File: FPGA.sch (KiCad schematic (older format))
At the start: 38 parts

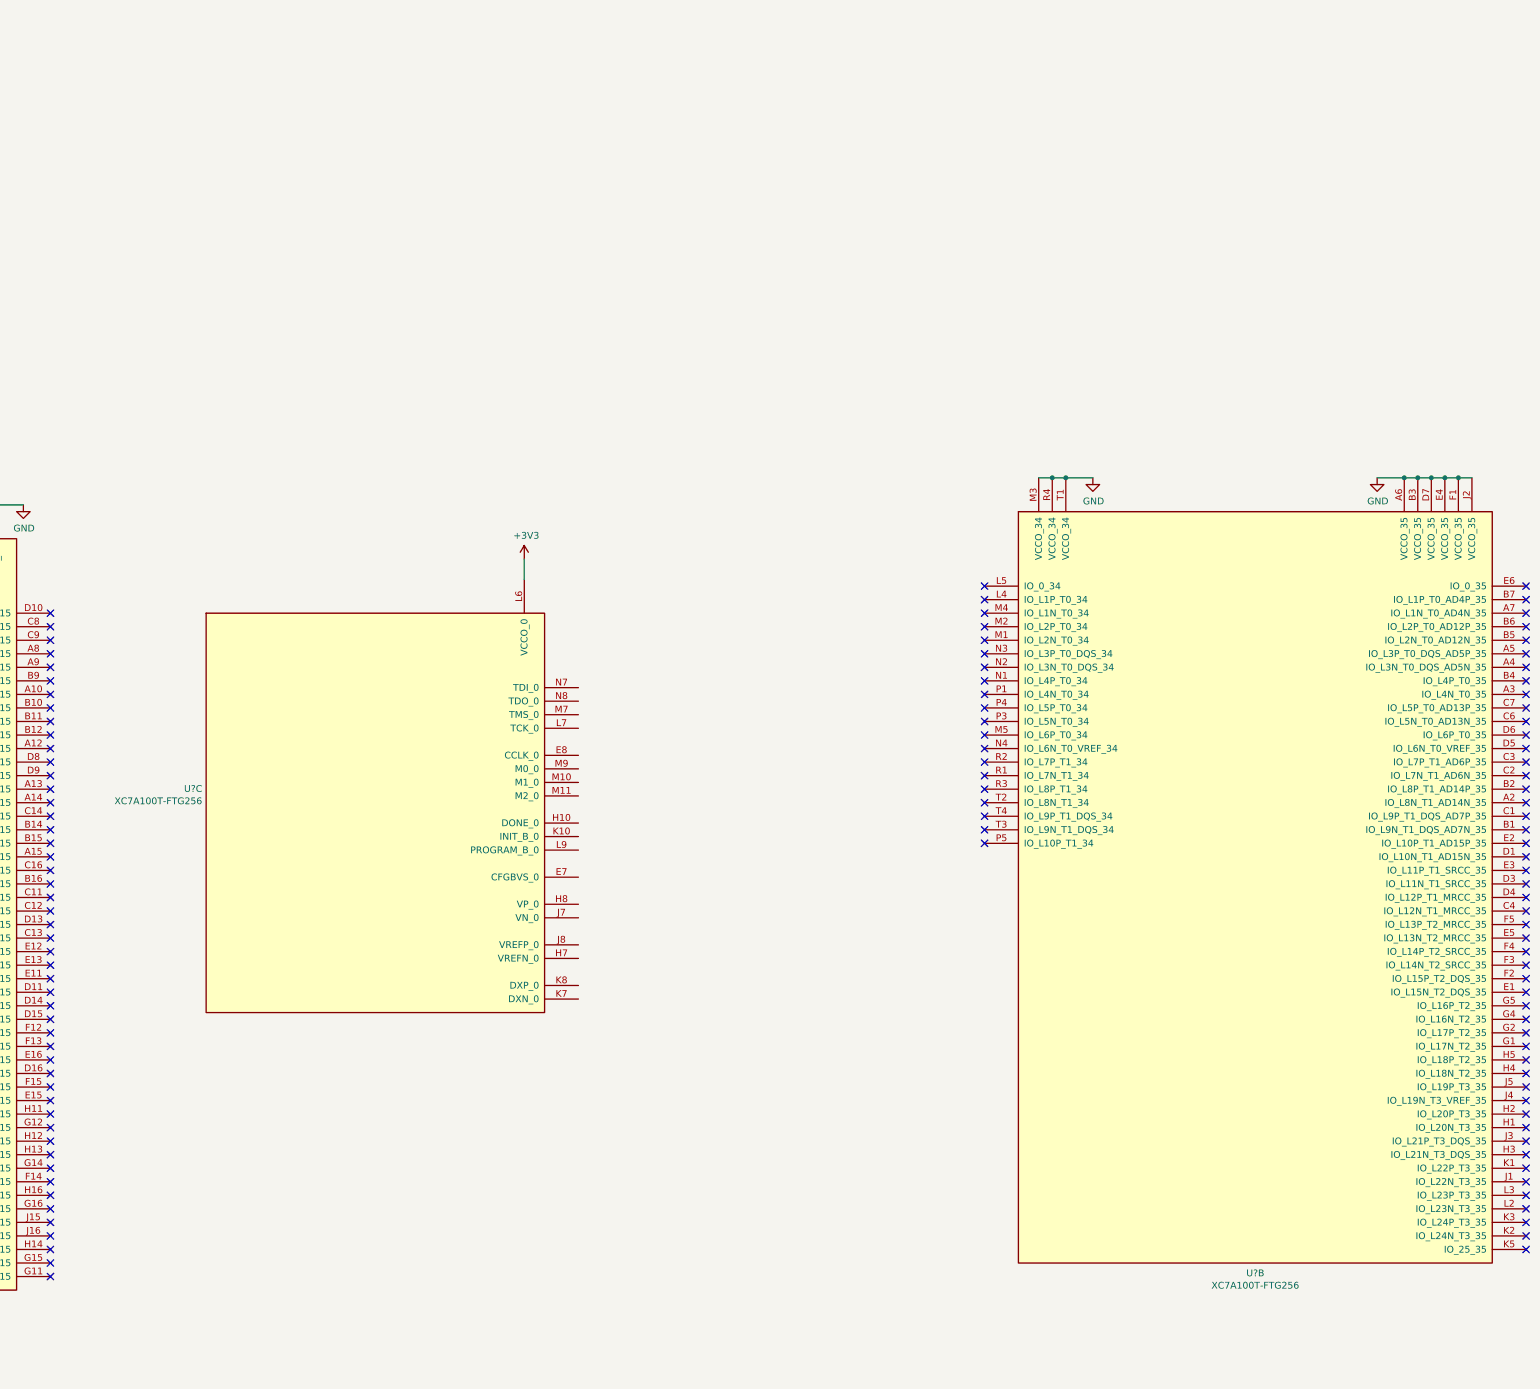
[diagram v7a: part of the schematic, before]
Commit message: Move FPGA JTAG schematic to subsheet
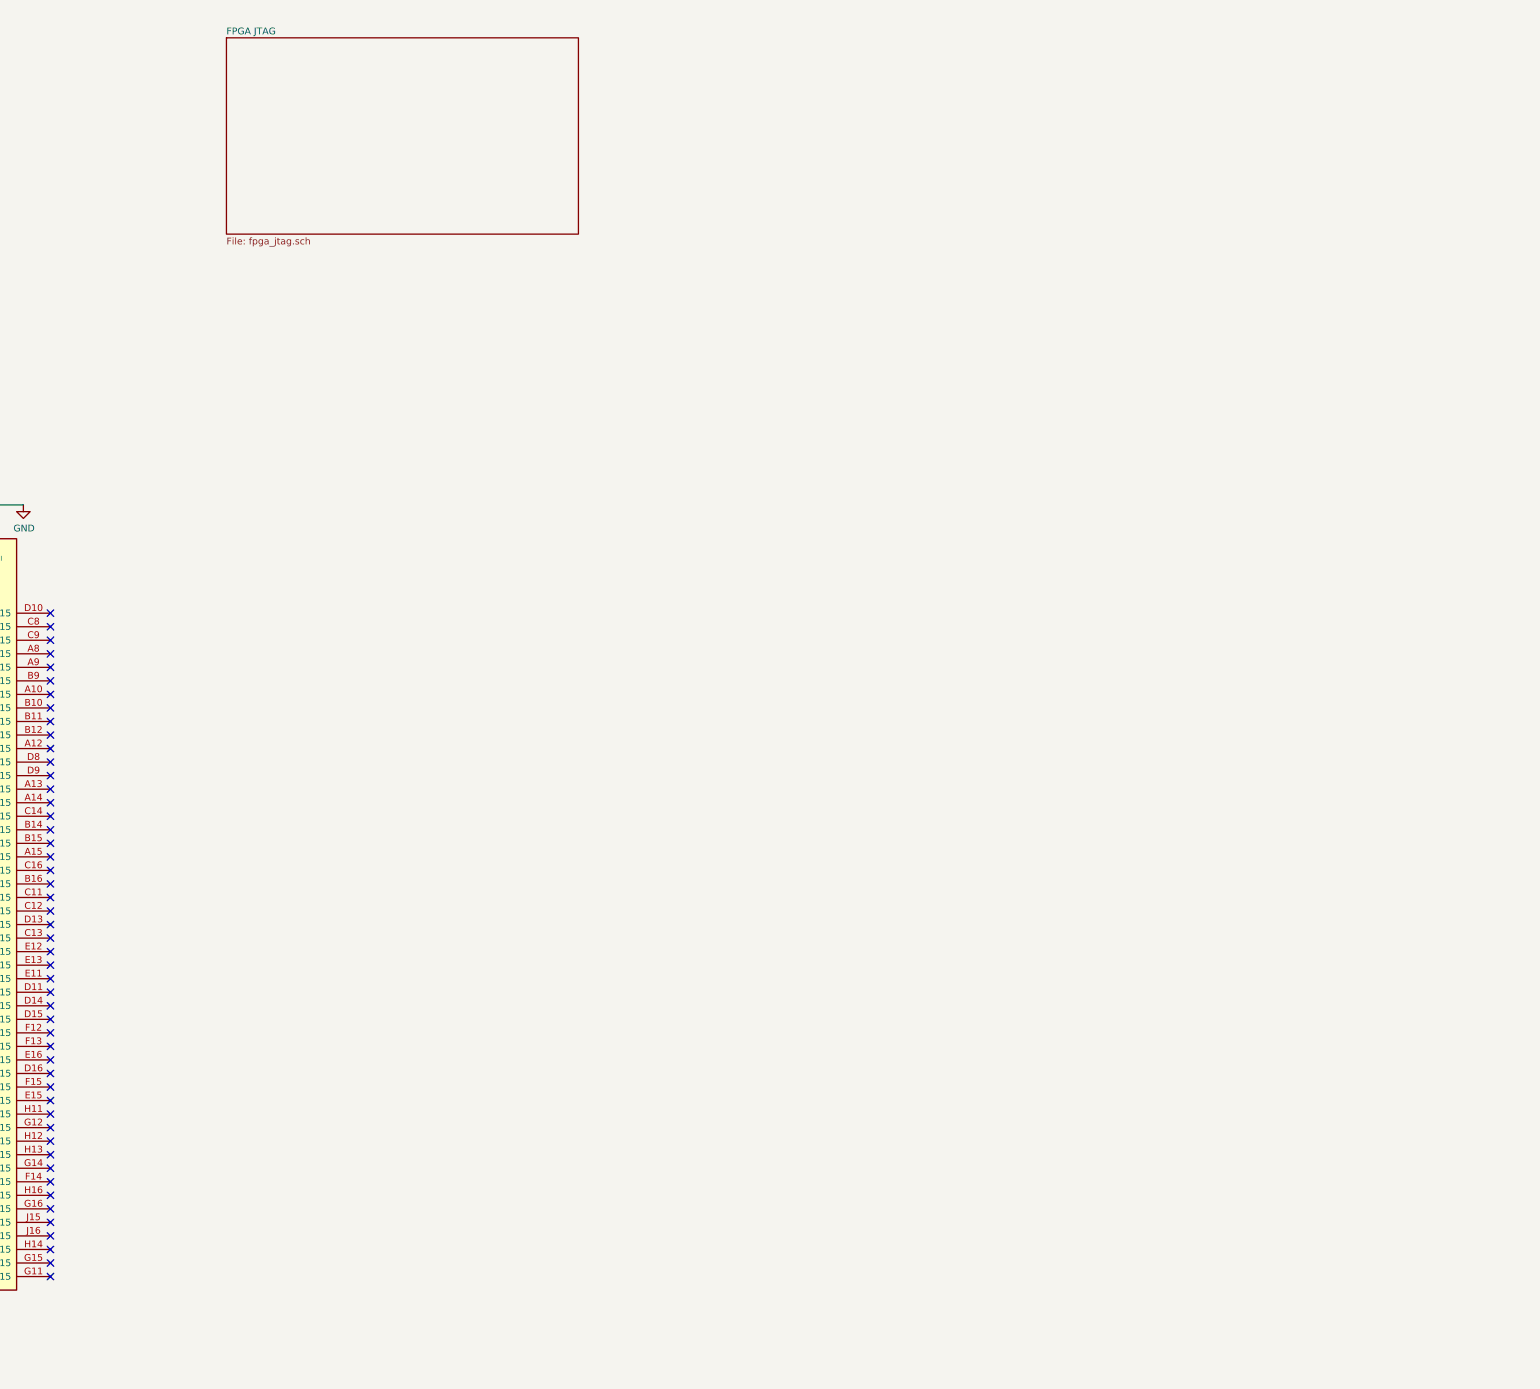
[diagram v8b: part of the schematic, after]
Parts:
- removed U? (x2): XC7A100T-FTG256, symbol FPGA_Xilinx_Artix7:XC7A100T-FTG256
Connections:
- no-connect marks 121 -> 51
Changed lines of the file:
@@
 $Descr A4 11693 8268
 encoding utf-8
-Sheet 2 5
+Sheet 2 6
 Title ""
 Date ""
@@
 $EndComp
 $Comp
-L FPGA_Xilinx_Artix7:XC7A100T-FTG256 U?
-U 3 1 5D914AF2
-P 8000 3150
-F 0 "U?" H 6721 3203 50  0000 R CNN
-F 1 "XC7A100T-FTG256" H 6721 3112 50  0000 R CNN
-F 2 "" H 8000 3150 50  0001 C CNN
-F 3 "" H 8000 3150 50  0000 C CNN
-	3    8000 3150
-	1    0    0    -1
-$EndComp
-$Comp
 L power:GND #PWR0101
 U 1 1 5D9CDED6
@@
 Connection ~ 6400 13000
 Connection ~ 6700 13000
-$Comp
-L power:+3V3 #PWR?
-U 1 1 5DC2583F
-P 9100 1400
-F 0 "#PWR?" H 9100 1250 50  0001 C CNN
-F 1 "+3V3" H 9115 1573 50  0000 C CNN
-F 2 "" H 9100 1400 50  0001 C CNN
-F 3 "" H 9100 1400 50  0001 C CNN
-	1    9100 1400
-	1    0    0    -1
-$EndComp
-Wire Wire Line
-	9100 1400 9100 1550
 $Comp
 L power:+3V3 #PWR?
@@
 NoConn ~ 5600 6700
 $Comp
-L FPGA_Xilinx_Artix7:XC7A100T-FTG256 U?
-U 2 1 5DC53F4D
-P 14500 3700
-F 0 "U?" H 14500 725 50  0000 C CNN
-F 1 "XC7A100T-FTG256" H 14500 634 50  0000 C CNN
-F 2 "" H 14500 3700 50  0001 C CNN
-F 3 "" H 14500 3700 50  0000 C CNN
-	2    14500 3700
-	1    0    0    -1
-$EndComp
-$Comp
-L power:GND #PWR?
-U 1 1 5DC60A9F
-P 13300 800
-F 0 "#PWR?" H 13300 550 50  0001 C CNN
-F 1 "GND" H 13305 627 50  0000 C CNN
-F 2 "" H 13300 800 50  0001 C CNN
-F 3 "" H 13300 800 50  0001 C CNN
-	1    13300 800
-	1    0    0    -1
-$EndComp
-$Comp
-L power:GND #PWR?
-U 1 1 5DC61257
-P 15400 800
-F 0 "#PWR?" H 15400 550 50  0001 C CNN
-F 1 "GND" H 15405 627 50  0000 C CNN
-F 2 "" H 15400 800 50  0001 C CNN
-F 3 "" H 15400 800 50  0001 C CNN
-	1    15400 800
-	1    0    0    -1
-$EndComp
-Wire Wire Line
-	15400 800  15600 800
-Connection ~ 15600 800
-Wire Wire Line
-	15600 800  15700 800
-Connection ~ 15700 800
-Wire Wire Line
-	15700 800  15800 800
-Connection ~ 15800 800
-Wire Wire Line
-	15800 800  15900 800
-Connection ~ 15900 800
-Wire Wire Line
-	15900 800  16000 800
-Connection ~ 16000 800
-Wire Wire Line
-	16000 800  16100 800
-Wire Wire Line
-	12900 800  13000 800
-Connection ~ 13000 800
-Wire Wire Line
-	13000 800  13100 800
-Connection ~ 13100 800
-Wire Wire Line
-	13100 800  13300 800
-NoConn ~ 12500 1600
-NoConn ~ 12500 1700
-NoConn ~ 12500 1800
-NoConn ~ 12500 1900
-NoConn ~ 12500 2000
-NoConn ~ 12500 2100
-NoConn ~ 12500 2200
-NoConn ~ 12500 2300
-NoConn ~ 12500 2400
-NoConn ~ 12500 2500
-NoConn ~ 12500 2600
-NoConn ~ 12500 2700
-NoConn ~ 12500 2800
-NoConn ~ 12500 2900
-NoConn ~ 12500 3000
-NoConn ~ 12500 3100
-NoConn ~ 12500 3200
-NoConn ~ 12500 3300
-NoConn ~ 12500 3400
-NoConn ~ 12500 3500
-NoConn ~ 16500 1600
-NoConn ~ 16500 1700
-NoConn ~ 16500 1800
-NoConn ~ 16500 1900
-NoConn ~ 16500 2000
-NoConn ~ 16500 2100
-NoConn ~ 16500 2200
-NoConn ~ 16500 2300
-NoConn ~ 16500 2400
-NoConn ~ 16500 2500
-NoConn ~ 16500 2600
-NoConn ~ 16500 2700
-NoConn ~ 16500 2800
-NoConn ~ 16500 2900
-NoConn ~ 16500 3000
-NoConn ~ 16500 3100
-NoConn ~ 16500 3200
-NoConn ~ 16500 3300
-NoConn ~ 16500 3400
-NoConn ~ 16500 3500
-NoConn ~ 16500 3600
-NoConn ~ 16500 3700
-NoConn ~ 16500 3800
-NoConn ~ 16500 3900
-NoConn ~ 16500 4000
-NoConn ~ 16500 4100
-NoConn ~ 16500 4200
-NoConn ~ 16500 4300
-NoConn ~ 16500 4400
-NoConn ~ 16500 4500
-NoConn ~ 16500 4600
-NoConn ~ 16500 4700
-NoConn ~ 16500 4800
-NoConn ~ 16500 4900
-NoConn ~ 16500 5000
-NoConn ~ 16500 5100
-NoConn ~ 16500 5200
-NoConn ~ 16500 5300
-NoConn ~ 16500 5400
-NoConn ~ 16500 5500
-NoConn ~ 16500 5600
-NoConn ~ 16500 5700
-NoConn ~ 16500 5800
-NoConn ~ 16500 5900
-NoConn ~ 16500 6000
-NoConn ~ 16500 6100
-NoConn ~ 16500 6200
-NoConn ~ 16500 6300
-NoConn ~ 16500 6400
-NoConn ~ 16500 6500
-$Comp
 L power:GND #PWR?
 U 1 1 5DE9DE35
@@
 Connection ~ 1150 4500
 Connection ~ 1150 4800
+$Sheet
+S 6900 -2450 2600 1450
+U 5DD5155F
+F0 "FPGA JTAG" 50
+F1 "fpga_jtag.sch" 50
+$EndSheet
 $EndSCHEMATC
